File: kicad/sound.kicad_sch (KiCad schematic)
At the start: 16 parts, among them J4 Speaker, U17 LM386, U3 AY-3-8912, U33 ZAK181AY (GAL16V8)

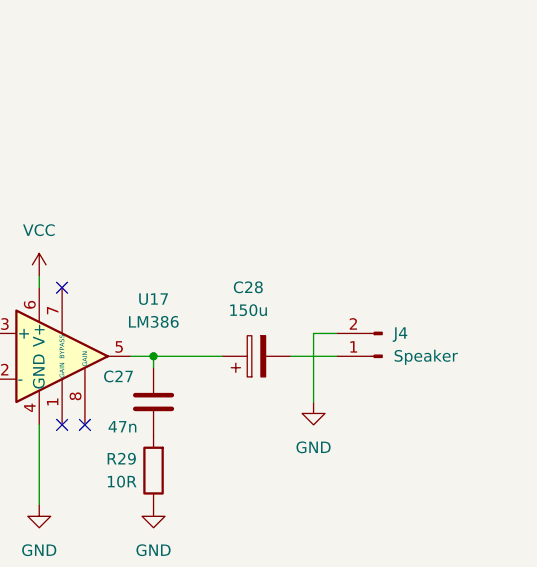
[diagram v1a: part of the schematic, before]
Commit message: rev D
- Fix SUB-D footprints yet again,
- rotate keyboard connector to remove cable twist,
- add onboard speaker.
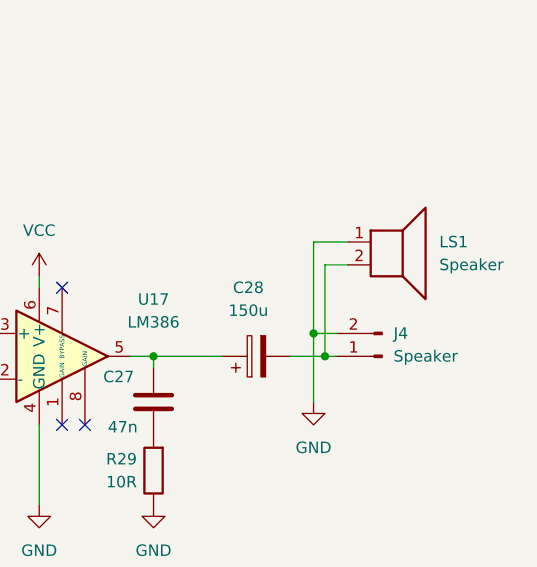
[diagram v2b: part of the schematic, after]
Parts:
- added LS1: Speaker, Buzzer_Beeper:MagneticBuzzer_StarMicronics_QMB-105, symbol Device:Speaker
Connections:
- net GND: now also LS1.1
- net at C28.2, J4.1 (Pin_1): now also LS1.2
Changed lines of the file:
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@@
 	(title_block
 		(title "Sound")
-		(date "2025-07-20")
-		(rev "C")
+		(date "2025-08-02")
+		(rev "D")
 		(company "A.K.")
 	)
@@
 	)
 	(junction
+		(at 231.14 81.28)
+		(diameter 0)
+		(color 0 0 0 0)
+	)
+	(junction
 		(at 77.47 110.49)
 		(diameter 0)
@@
 	)
 	(junction
+		(at 232.41 83.82)
+		(diameter 0)
+		(color 0 0 0 0)
+	)
+	(junction
 		(at 173.99 81.28)
 		(diameter 0)
@@
 		)
 	)
+	(wire
+		(pts
+			(xy 232.41 83.82) (xy 233.68 83.82)
+		)
+		(stroke
+			(width 0)
+			(type default)
+		)
+	)
 	(bus
 		(pts
@@
 	(wire
 		(pts
+			(xy 234.95 71.12) (xy 231.14 71.12)
+		)
+		(stroke
+			(width 0)
+			(type default)
+		)
+	)
+	(wire
+		(pts
 			(xy 173.99 76.2) (xy 181.61 76.2)
 		)
@@
 	(wire
 		(pts
-			(xy 228.6 83.82) (xy 233.68 83.82)
+			(xy 228.6 83.82) (xy 232.41 83.82)
 		)
 		(stroke
@@
 	(wire
 		(pts
+			(xy 232.41 83.82) (xy 232.41 73.66)
+		)
+		(stroke
+			(width 0)
+			(type default)
+		)
+	)
+	(wire
+		(pts
 			(xy 181.61 86.36) (xy 195.58 86.36)
 		)
@@
 	(wire
 		(pts
+			(xy 232.41 73.66) (xy 234.95 73.66)
+		)
+		(stroke
+			(width 0)
+			(type default)
+		)
+	)
+	(wire
+		(pts
 			(xy 116.84 97.79) (xy 121.92 97.79)
 		)
@@
 		(pts
 			(xy 76.2 115.57) (xy 78.74 115.57)
+		)
+		(stroke
+			(width 0)
+			(type default)
+		)
+	)
+	(wire
+		(pts
+			(xy 231.14 71.12) (xy 231.14 81.28)
 		)
 		(stroke
@@
 					(unit 1)
 				)
+			)
+		)
+	)
+	(symbol
+		(lib_id "Device:Speaker")
+		(at 240.03 71.12 0)
+		(unit 1)
+		(exclude_from_sim no)
+		(in_bom yes)
+		(on_board yes)
+		(dnp no)
+		(fields_autoplaced yes)
+		(property "Reference" "LS1"
+			(at 245.11 71.1199 0)
+			(effects
+				(font
+					(size 1.27 1.27)
+				)
+				(justify left)
+			)
+		)
+		(property "Value" "Speaker"
+			(at 245.11 73.6599 0)
+			(effects
+				(font
+					(size 1.27 1.27)
+				)
+				(justify left)
+			)
+		)
+		(property "Footprint" "Buzzer_Beeper:MagneticBuzzer_StarMicronics_QMB-105"
+			(at 240.03 76.2 0)
+			(effects
+				(font
+					(size 1.27 1.27)
+				)
+				(hide yes)
+			)
+		)
+		(property "Datasheet" "~"
+			(at 239.776 72.39 0)
+			(effects
+				(font
+					(size 1.27 1.27)
+				)
+				(hide yes)
+			)
+		)
+		(property "Description" "Speaker"
+			(at 240.03 71.12 0)
+			(effects
+				(font
+					(size 1.27 1.27)
+				)
+				(hide yes)
+			)
+		)
+		(pin "1"
+		)
+		(pin "2"
+		)
+		(instances
+			(project ""
+				(path "/ca48b56d-33a4-442b-b1b9-aaf2c2c8d68d/0bc6fd8f-001b-40d5-aa7a-728fb33c946c"
+					(reference "LS1")
+					(unit 1)
+				)
